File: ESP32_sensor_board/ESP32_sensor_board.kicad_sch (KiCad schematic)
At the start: 25 parts, among them J1 SS-52400-003, J2 B2B-PH-SM4-TB, U1 MCP73871

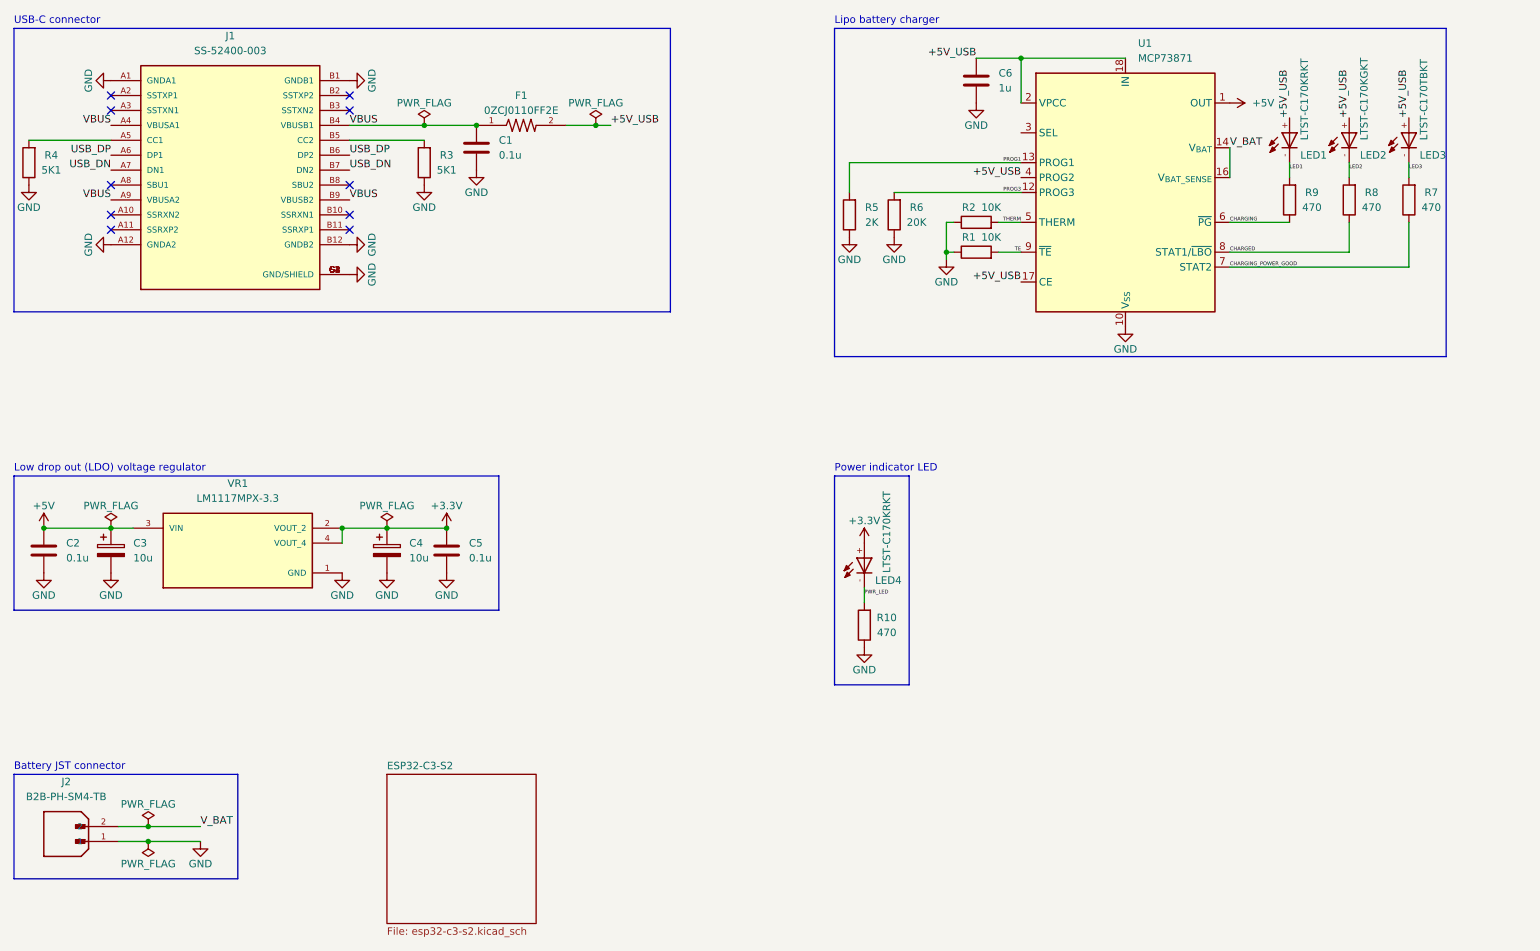
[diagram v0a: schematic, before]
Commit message: Schematic design section 2 completed
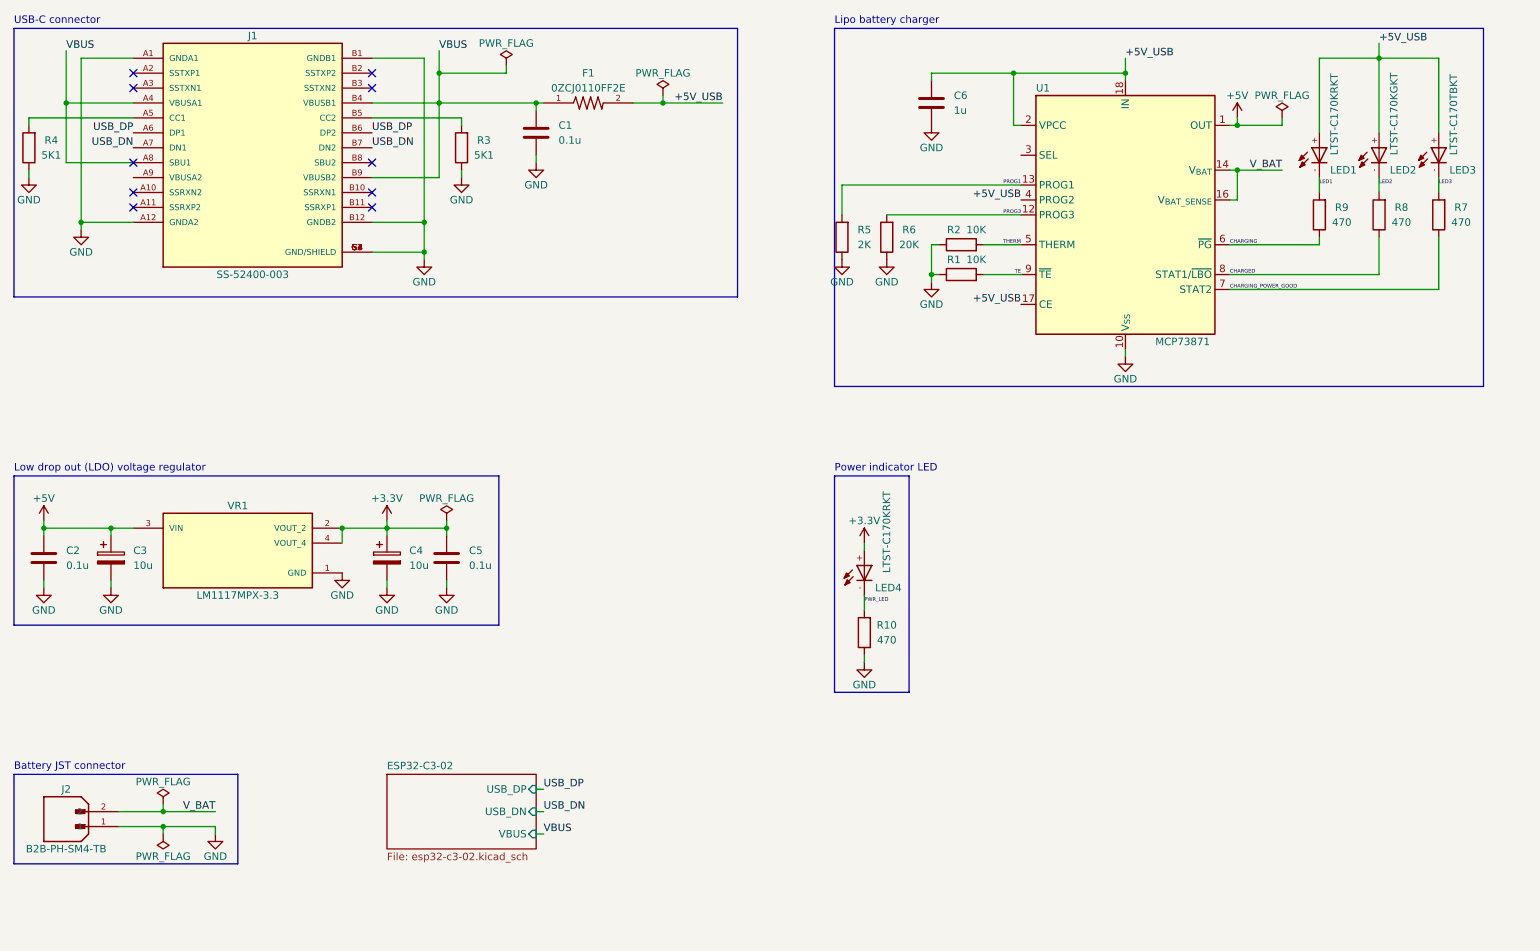
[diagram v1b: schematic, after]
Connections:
- net VBUS: now also J1.A8 (SBU1); no longer J1.A9 (VBUSA2)
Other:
- sheet ESP32-C3-S2 renamed ESP32-C3-02
- sheet ESP32-C3-02: file esp32-c3-s2.kicad_sch -> esp32-c3-02.kicad_sch
- sheet ESP32-C3-02 ports: added USB_DN, USB_DP, VBUS; removed none
- moved on the sheet: C1, C2, C3, C4, C5, C6, F1, J1, J2, LED1, LED2, LED3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

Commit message: Schematic design section 3 completed
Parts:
- C1, C2, C5, C6: footprint (none) -> Capacitor_SMD:C_0805_2012Metric
- C3, C4: footprint (none) -> footprints:T491A106K010AT
- F1: footprint 0ZCJ0110FF2E:RESC3216X125N -> footprints:RESC3216X125N
- J1: footprint SS-52400-003:BELFUSE_SS-52400-003 -> footprints:BELFUSE_SS-52400-003
- J2: footprint B2B-PH-SM4-TB:JST_B2B-PH-SM4-TB -> footprints:JST_B2B-PH-SM4-TB
- LED1, LED4: footprint LTST-C170KRKT:DIOC200X125X110 -> footprints:DIOC200X125X110
- LED2: footprint LTST-C170KGKT:DIOC200X125X110 -> footprints:DIOC200X125X110
- LED3: footprint LTST-C170TBKT:DIOC200X125X110 -> footprints:DIOC200X125X110
- R1, R10, R2, R3, R4, R5, R6, R7, R8, R9: footprint (none) -> Resistor_SMD:R_0805_2012Metric
- VR1: footprint LM1117MPX-3.3:VREG_LM1117MPX-3.3 -> footprints:VREG_LM1117MPX-3.3
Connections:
- net GND: now also U1.3 (SEL)
- net VBUS: now also J1.A9 (VBUSA2); no longer J1.A8 (SBU1)
- net V_BAT renamed VBAT
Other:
- moved on the sheet: C1, C2, C5, C6, F1, J1, LED1, LED2, LED3, R1, R2, R3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

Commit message: Layout design section 2 completed
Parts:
- added H1, H2, H3: MountingHole, MountingHole:MountingHole_2.5mm, symbol Mechanical:MountingHole
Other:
- note added: "Mechanical"
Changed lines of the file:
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@@
 	)
 	(rectangle
+		(start 215.9 101.6)
+		(end 251.46 127)
+		(stroke
+			(width 0)
+			(type default)
+		)
+		(fill
+			(type none)
+		)
+	)
+	(rectangle
 		(start 25.4 25.4)
 		(end 146.05 69.85)
@@
 		)
 	)
+	(text "Mechanical"
+		(exclude_from_sim no)
+		(at 215.9 100.33 0)
+		(effects
+			(font
+				(size 1.27 1.27)
+			)
+			(justify left)
+		)
+	)
 	(text "Low drop out (LDO) voltage regulator"
 		(exclude_from_sim no)
@@
 	)
 	(symbol
+		(lib_id "Mechanical:MountingHole")
+		(at 233.68 120.65 0)
+		(unit 1)
+		(exclude_from_sim no)
+		(in_bom no)
+		(on_board yes)
+		(dnp no)
+		(property "Reference" "H3"
+			(at 236.22 119.3799 0)
+			(effects
+				(font
+					(size 1.27 1.27)
+				)
+				(justify left)
+			)
+		)
+		(property "Value" "MountingHole"
+			(at 236.22 121.9199 0)
+			(effects
+				(font
+					(size 1.27 1.27)
+				)
+				(justify left)
+			)
+		)
+		(property "Footprint" "MountingHole:MountingHole_2.5mm"
+			(at 233.68 124.46 0)
+			(effects
+				(font
+					(size 1.27 1.27)
+				)
+			)
+		)
+		(property "Datasheet" "~"
+			(at 233.68 120.65 0)
+			(effects
+				(font
+					(size 1.27 1.27)
+				)
+				(hide yes)
+			)
+		)
+		(property "Description" "Mounting Hole without connection"
+			(at 233.68 120.65 0)
+			(effects
+				(font
+					(size 1.27 1.27)
+				)
+				(hide yes)
+			)
+		)
+		(instances
+			(project "ESP32_sensor_board"
+				(path "/a7c0144a-eab4-4f71-87a7-133855887b73"
+					(reference "H3")
+					(unit 1)
+				)
+			)
+		)
+	)
+	(symbol
 		(lib_id "Device:R")
 		(at 100.33 45.72 180)
@@
 	)
 	(symbol
+		(lib_id "Mechanical:MountingHole")
+		(at 233.68 105.41 0)
+		(unit 1)
+		(exclude_from_sim no)
+		(in_bom no)
+		(on_board yes)
+		(dnp no)
+		(property "Reference" "H1"
+			(at 236.22 104.1399 0)
+			(effects
+				(font
+					(size 1.27 1.27)
+				)
+				(justify left)
+			)
+		)
+		(property "Value" "MountingHole"
+			(at 236.22 106.6799 0)
+			(effects
+				(font
+					(size 1.27 1.27)
+				)
+				(justify left)
+			)
+		)
+		(property "Footprint" "MountingHole:MountingHole_2.5mm"
+			(at 233.68 109.22 0)
+			(effects
+				(font
+					(size 1.27 1.27)
+				)
+			)
+		)
+		(property "Datasheet" "~"
+			(at 233.68 105.41 0)
+			(effects
+				(font
+					(size 1.27 1.27)
+				)
+				(hide yes)
+			)
+		)
+		(property "Description" "Mounting Hole without connection"
+			(at 233.68 105.41 0)
+			(effects
+				(font
+					(size 1.27 1.27)
+				)
+				(hide yes)
+			)
+		)
+		(instances
+			(project ""
+				(path "/a7c0144a-eab4-4f71-87a7-133855887b73"
+					(reference "H1")
+					(unit 1)
+				)
+			)
+		)
+	)
+	(symbol
 		(lib_id "power:+3.3V")
 		(at 170.18 113.03 0)
@@
 					(unit 1)
 				)
+			)
+		)
+	)
+	(symbol
+		(lib_id "Mechanical:MountingHole")
+		(at 233.68 113.03 0)
+		(unit 1)
+		(exclude_from_sim no)
+		(in_bom no)
+		(on_board yes)
+		(dnp no)
+		(property "Reference" "H2"
+			(at 236.22 111.7599 0)
+			(effects
+				(font
+					(size 1.27 1.27)
+				)
+				(justify left)
+			)
+		)
+		(property "Value" "MountingHole"
+			(at 236.22 114.2999 0)
+			(effects
+				(font
+					(size 1.27 1.27)
+				)
+				(justify left)
+			)
+		)
+		(property "Footprint" "MountingHole:MountingHole_2.5mm"
+			(at 233.68 116.84 0)
+			(effects
+				(font
+					(size 1.27 1.27)
+				)
+			)
+		)
+		(property "Datasheet" "~"
+			(at 233.68 113.03 0)
+			(effects
+				(font
+					(size 1.27 1.27)
+				)
+				(hide yes)
+			)
+		)
+		(property "Description" "Mounting Hole without connection"
+			(at 233.68 113.03 0)
+			(effects
+				(font
+					(size 1.27 1.27)
+				)
+				(hide yes)
+			)
+		)
+		(instances
+			(project "ESP32_sensor_board"
+				(path "/a7c0144a-eab4-4f71-87a7-133855887b73"
+					(reference "H2")
+					(unit 1)
+				)

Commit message: Layout design section 3 in progress
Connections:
- net CC2: now reaches J1.B5 (CC2), R3.2
- net CC1: now reaches J1.A5 (CC1), R4.2
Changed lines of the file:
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@@
+		)
+	)
+	(label "CC1"
+		(at 44.45 40.64 180)
+		(effects
+			(font
+				(size 0.63 0.63)
+			)
+			(justify right bottom)
 		)
 	)
@@
 			)
 			(justify left bottom)
+		)
+	)
+	(label "CC2"
+		(at 85.09 40.64 0)
+		(effects
+			(font
+				(size 0.63 0.63)
+			)
+			(justify left bottom)

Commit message: Prototype 2 completed
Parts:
- added F2: 0ZCJ0110FF2E, footprints:RESC3216X125N, symbol 0ZCJ0110FF2E:0ZCJ0110FF2E
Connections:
- net +5V: now also F2.2; no longer U1.1 (OUT), U1.20 (OUT)
- new net OUT: F2.1, U1.1 (OUT), U1.20 (OUT)
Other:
- moved on the sheet: LED1, LED2, LED3, R7, R8, R9
